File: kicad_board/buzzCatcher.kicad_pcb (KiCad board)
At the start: 2 copper layers, 63 x 100 mm, 31 parts, among them IC1 CD4043BE-NG, IC2 COM-16473, IC3 CD74HCT173E, IC4 CD4072BE, IC5 SN74LS04N, IC6 SN74LS21NE4, IC7 TS02-66-60-BK-100-SCR-D, J1 154-UL6661, J2 154-UL6661, J3 154-UL6661, J4 154-UL6661, J5 USB4130-GF-C, Q1 BS170

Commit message: Arduino version
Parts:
- removed C1, C3: 3.3 nF, SamacSys_PCB_Library:ECWH16362RJV
- removed C2: 10 uF, SamacSys_PCB_Library:CAPPRD250W65D630H900
- removed D1, D2, D3, D4, D5: LED, LED_THT:LED_D3.0mm_Horizontal_O6.35mm_Z2.0mm
- removed IC2: COM-16473, SamacSys_PCB_Library:DIP794W53P254L959H508Q8N
- removed IC3: CD74HCT173E, SamacSys_PCB_Library:DIP794W53P254L1930H508Q16N
- removed IC4: CD4072BE, SamacSys_PCB_Library:DIP794W53P254L1930H508Q14N
- removed IC5: SN74LS04N, SamacSys_PCB_Library:DIP794W53P254L1930H508Q14N
- removed IC6: SN74LS21NE4, SamacSys_PCB_Library:DIP794W53P254L1930H508Q14N
- removed IC7: TS02-66-60-BK-100-SCR-D, SamacSys_PCB_Library:TS026660BK100SCRD
- removed J5: USB4130-GF-C, SamacSys_PCB_Library:USB4130GFC
- removed R1, R8: 110k, Resistor_THT:R_Axial_DIN0207_L6.3mm_D2.5mm_P10.16mm_Horizontal
- removed R2, R3, R4, R5, R6: 300, Resistor_THT:R_Axial_DIN0207_L6.3mm_D2.5mm_P15.24mm_Horizontal
- removed R7: 0, Resistor_THT:R_Axial_DIN0207_L6.3mm_D2.5mm_P10.16mm_Horizontal
- added A1: Arduino_Nano_v3.x, Module:Arduino_Nano, F.Cu at (75.0, 99.9)
- added LED9: SSA-LXH1025GD, SamacSys_PCB_Library:SSALXH1025GD, F.Cu at (100.0, 134.5)
- added Q2: BS170, SamacSys_PCB_Library:LM431ACZ, F.Cu at (85.4, 75.6)
- added RN1: EXB2HV103JV, SamacSys_PCB_Library:EXB2HV104JV, F.Cu at (94.5, 81.5)
- added RN2: EXB2HV121JV, SamacSys_PCB_Library:EXB2HV_1, F.Cu at (91.7, 91.3)
- added RN3: EXB2HV121JV, SamacSys_PCB_Library:EXB2HV_1, F.Cu at (90.0, 81.5)
- IC1: value CD4043BE-NG -> TS02-66-60-BK-100-SCR-D; footprint SamacSys_PCB_Library:DIP794W53P254L1930H508Q16N -> SamacSys_PCB_Library:TS026660BK100SCRD
- J1, J2, J3, J4: value 154-UL6661 -> 95501-2661; footprint SamacSys_PCB_Library:154UL6661 -> SamacSys_PCB_Library:95501-2661
- moved Q1 70.0 mm to (75.3, 75.7), turned to 180 degrees
- moved S1 66.4 mm to (95.0, 71.0)
- moved LS1 51.3 mm to (80.0, 90.0)
- moved J1 42.8 mm to (60.0, 90.0), turned to -90 degrees
- moved J2 41.8 mm to (60.0, 105.2), turned to -90 degrees
- moved J3 40.7 mm to (60.0, 120.2), turned to -90 degrees
- moved J4 39.4 mm to (60.0, 134.4), turned to -90 degrees
- moved IC1 20.5 mm to (58.8, 68.8), turned to 0 degrees
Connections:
- IC1 pad 2: /listening_state* -> unconnected-(IC1-NO_2-Pad2)
- IC1 pad 3: /reset_button -> /Button 1
- IC1 pad 4: Net-(IC1-S1) -> /Vbus_5V
- J1 pad 3: /trigger_1 -> /Trigger 1
- J1 pad 4: Net-(IC5-1Y) -> Net-(Q1-SOURCE)
- J2 pad 3: /trigger_2 -> /Trigger 2
- J2 pad 4: Net-(IC5-2Y) -> Net-(Q1-SOURCE)
- J3 pad 3: /trigger_3 -> /Trigger 3
- J3 pad 4: Net-(IC5-3Y) -> Net-(Q1-SOURCE)
- J4 pad 3: /trigger_4 -> /Trigger 4
- J4 pad 4: Net-(IC5-4Y) -> Net-(Q1-SOURCE)
- Q1 pad 2: Net-(IC6-1Y) -> /Ready
- Q1 pad 3: Net-(LS1-+) -> Net-(Q1-SOURCE)
- S1 pad 2: Net-(IC6-1C) -> /Switch 1
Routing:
- net /Button 1: track 0.00 -> 107.4 mm
- net /Switch 1: track 0.00 -> 78.5 mm
- net /Trigger 1: track 0.00 -> 73.1 mm, vias 0 -> 1
- net /Buzzer: track 0.00 -> 70.1 mm, vias 0 -> 1
- net /Trigger 2: track 0.00 -> 61.8 mm, vias 0 -> 1
- net Net-(Q1-SOURCE): track 0.00 -> 60.9 mm
- net Net-(IC2-OUT): track 59.3 -> 0.00 mm
- net /Trigger 4: track 0.00 -> 58.1 mm, vias 0 -> 1
- net /Ready: track 0.00 -> 55.2 mm, vias 0 -> 1
- net /Trigger 3: track 0.00 -> 52.6 mm, vias 0 -> 1
- net Net-(IC5-1Y): track 45.3 -> 0.00 mm
- net /trigger_4: track 44.9 -> 0.00 mm
- net /trigger_1: track 44.9 -> 0.00 mm
- net /trigger_3: track 44.8 -> 0.00 mm
- net /trigger_2: track 44.6 -> 0.00 mm
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- added copper zone on B.Cu, net /Vbus_5V
- added copper zone on F.Cu, net GND
- removed copper zone on F.Cu, net /Vbus_5V
- removed copper zone on B.Cu, net GND
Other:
- board size 63 x 100 mm -> 52.5 x 80 mm
- board text removed: "Player 1"
- board text removed: "Player 2"
- board text removed: "Player 3"
- board text removed: "Player 4"
- board text removed: "Power"
- board text removed: "Ready"
- board text removed: "Reset"
- board text removed: "Sound On/Off"

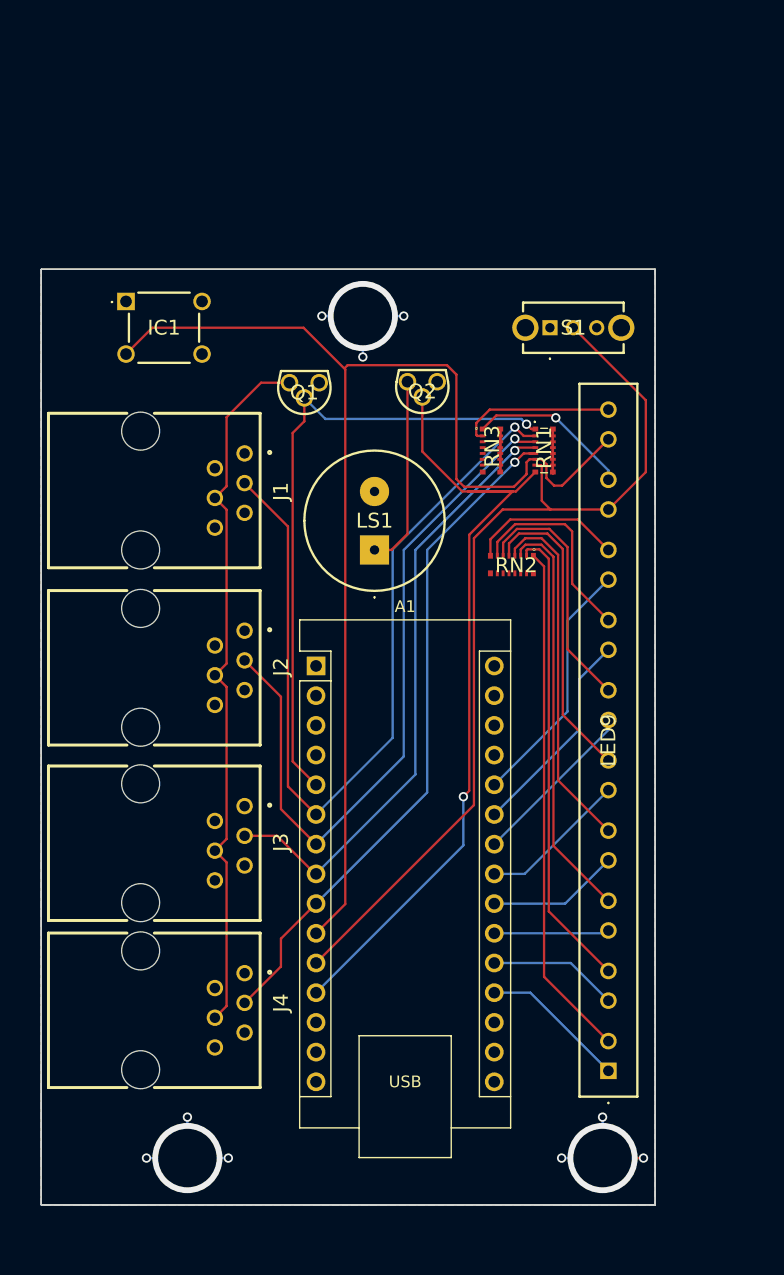
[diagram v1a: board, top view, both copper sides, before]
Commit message: Added break out headers
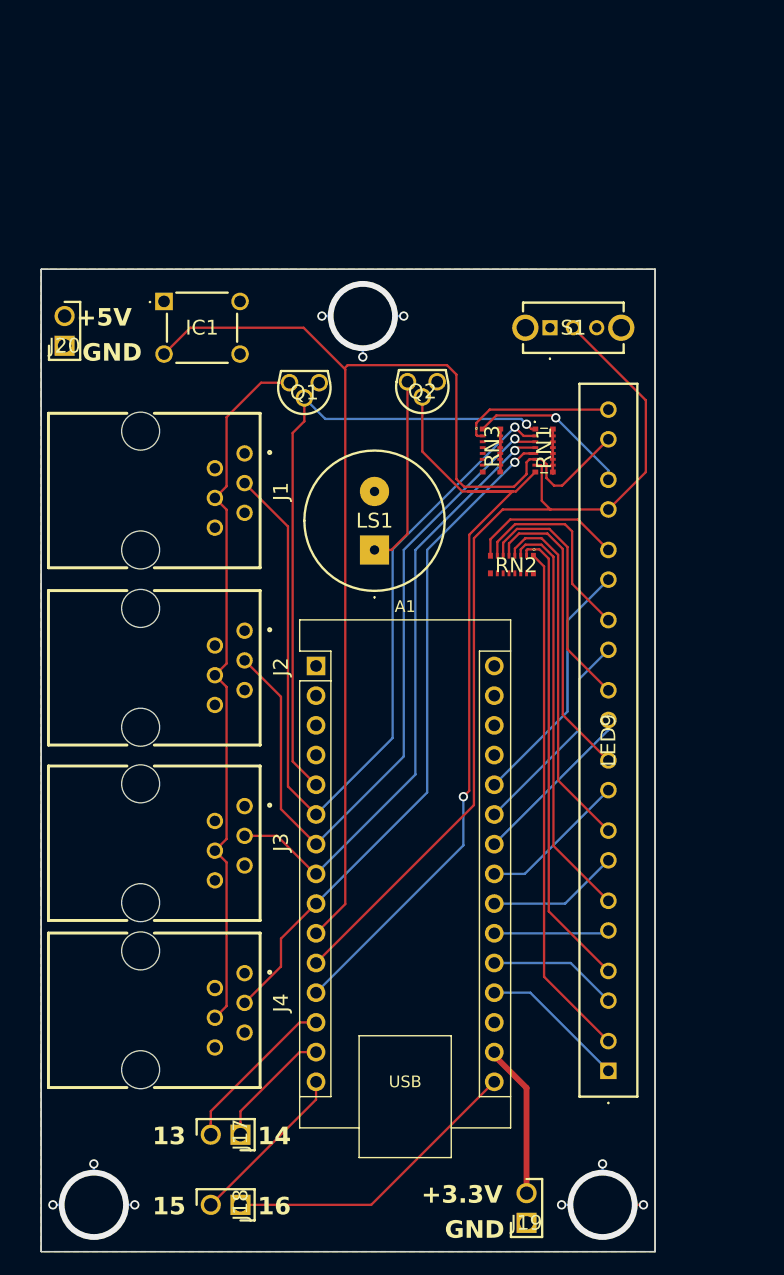
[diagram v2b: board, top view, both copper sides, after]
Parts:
- added J17: 67996-100HLF, SamacSys_PCB_Library:HDRV2W67P254_2X1_254X483X858P, F.Cu at (68.5, 140.0)
- added J18: 67996-100HLF, SamacSys_PCB_Library:HDRV2W67P254_2X1_254X483X858P, F.Cu at (68.5, 146.0)
- added J19: 67996-100HLF, SamacSys_PCB_Library:HDRV2W67P254_2X1_254X483X858P, F.Cu at (93.0, 147.5)
- added J20: 67996-100HLF, SamacSys_PCB_Library:HDRV2W67P254_2X1_254X483X858P, F.Cu at (53.5, 72.5)
- moved IC1 3.25 mm to (62.0, 68.8)
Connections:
- A1 pad 13: unconnected-(A1-D10-Pad13) -> Net-(A1-D10)
- A1 pad 14: unconnected-(A1-D11-Pad14) -> Net-(A1-D11)
- A1 pad 15: unconnected-(A1-D12-Pad15) -> Net-(A1-D12)
- A1 pad 16: unconnected-(A1-D13-Pad16) -> Net-(A1-D13)
- A1 pad 17: unconnected-(A1-3V3-Pad17) -> /Vbus_3V3
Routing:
- net Net-(A1-D13): track 0.00 -> 26.1 mm
- net Net-(A1-D10): track 0.00 -> 15.1 mm
- net Net-(A1-D12): track 0.00 -> 14.7 mm
- net /Vbus_3V3: track 0.00 -> 13.2 mm
- net Net-(A1-D11): track 0.00 -> 11.6 mm
- net /Button 1: track 107.4 -> 104.1 mm
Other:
- board size 52.5 x 80 mm -> 52.5 x 84 mm
- board text added: "+3.3V"
- board text added: "+5V"
- board text added: "13"
- board text added: "14"
- board text added: "15"
- board text added: "16"
- board text added: "GND"

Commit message: Converted to bigger resistor pack
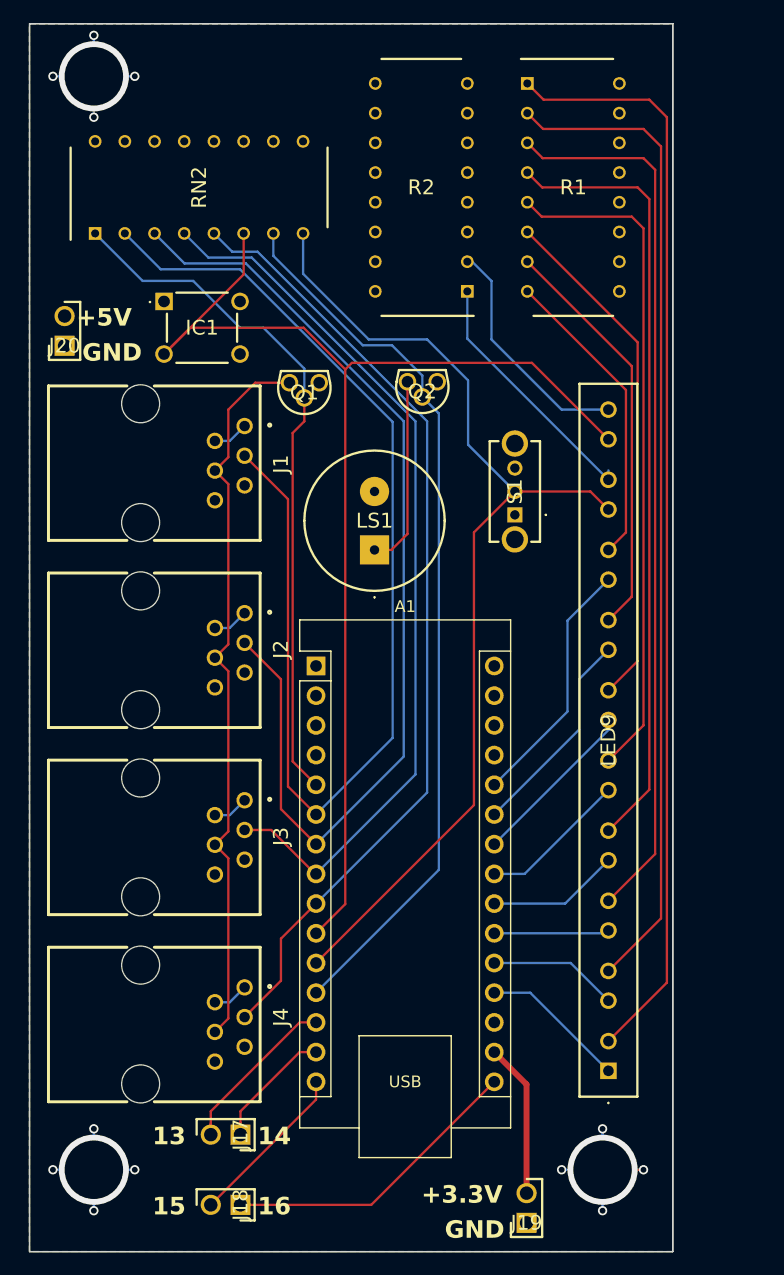
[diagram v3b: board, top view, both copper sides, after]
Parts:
- removed RN1: EXB2HV103JV, SamacSys_PCB_Library:EXB2HV104JV
- removed RN3: EXB2HV121JV, SamacSys_PCB_Library:EXB2HV_1
- added R1: 4116R-1-121LF, SamacSys_PCB_Library:DIP787W49P254L2197H469Q16N, F.Cu at (97.0, 59.0)
- added R2: 4116R-1-121LF, SamacSys_PCB_Library:DIP787W49P254L2197H469Q16N, F.Cu at (84.0, 59.0)
- RN2: value EXB2HV121JV -> 4116R-1-103FLF; footprint SamacSys_PCB_Library:EXB2HV_1 -> SamacSys_PCB_Library:DIP787W49P254L2197H469Q16N
- moved RN2 41.9 mm to (65.0, 59.0), turned to 90 degrees
- moved S1 16.3 mm to (92.0, 87.0), turned to 90 degrees
- moved J1 2.34 mm to (60.0, 87.7)
- moved J2 1.50 mm to (60.0, 103.7)
- moved J4 1.22 mm to (60.0, 135.7)
- moved J3 0.50 mm to (60.0, 119.7)
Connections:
- RN2 pad 1: Net-(LED9-K_1) -> /Ready
- RN2 pad 2: Net-(LED9-K_2) -> /Trigger 1
- RN2 pad 3: Net-(LED9-K_3) -> /Trigger 2
- RN2 pad 4: Net-(LED9-K_4) -> /Trigger 3
- RN2 pad 5: Net-(LED9-K_5) -> /Trigger 4
- RN2 pad 6: Net-(LED9-K_6) -> /Button 1
- RN2 pad 7: Net-(LED9-K_7) -> /Buzzer
- RN2 pad 8: Net-(LED9-K_8) -> /Switch 1
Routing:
- net Net-(LED9-K_1): track 44.2 -> 94.2 mm
- net Net-(LED9-K_2): track 40.1 -> 85.0 mm
- net Net-(LED9-K_3): track 35.3 -> 76.0 mm
- net Net-(LED9-K_4): track 30.6 -> 66.8 mm
- net Net-(LED9-K_5): track 26.2 -> 57.6 mm
- net /Trigger 1: track 73.1 -> 99.1 mm, vias 1 -> 0
- net /Trigger 2: track 61.8 -> 87.0 mm, vias 1 -> 0
- net /Trigger 4: track 58.1 -> 82.3 mm, vias 1 -> 0
- net /Trigger 3: track 52.6 -> 76.3 mm, vias 1 -> 0
- net Net-(LED9-K_6): track 21.4 -> 44.1 mm
- net Net-(LED9-K_7): track 17.3 -> 35.2 mm
- net GND: track 42.3 -> 57.8 mm, vias 12 -> 15
- net Net-(LED9-K_8): track 13.3 -> 26.2 mm
- net /Switch 1: track 78.5 -> 88.5 mm
- net Net-(LED9-K_9): track 14.0 -> 21.9 mm, vias 1 -> 0
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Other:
- board size 52.5 x 84 mm -> 55 x 105 mm

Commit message: Compacted to 100 x 50 mm
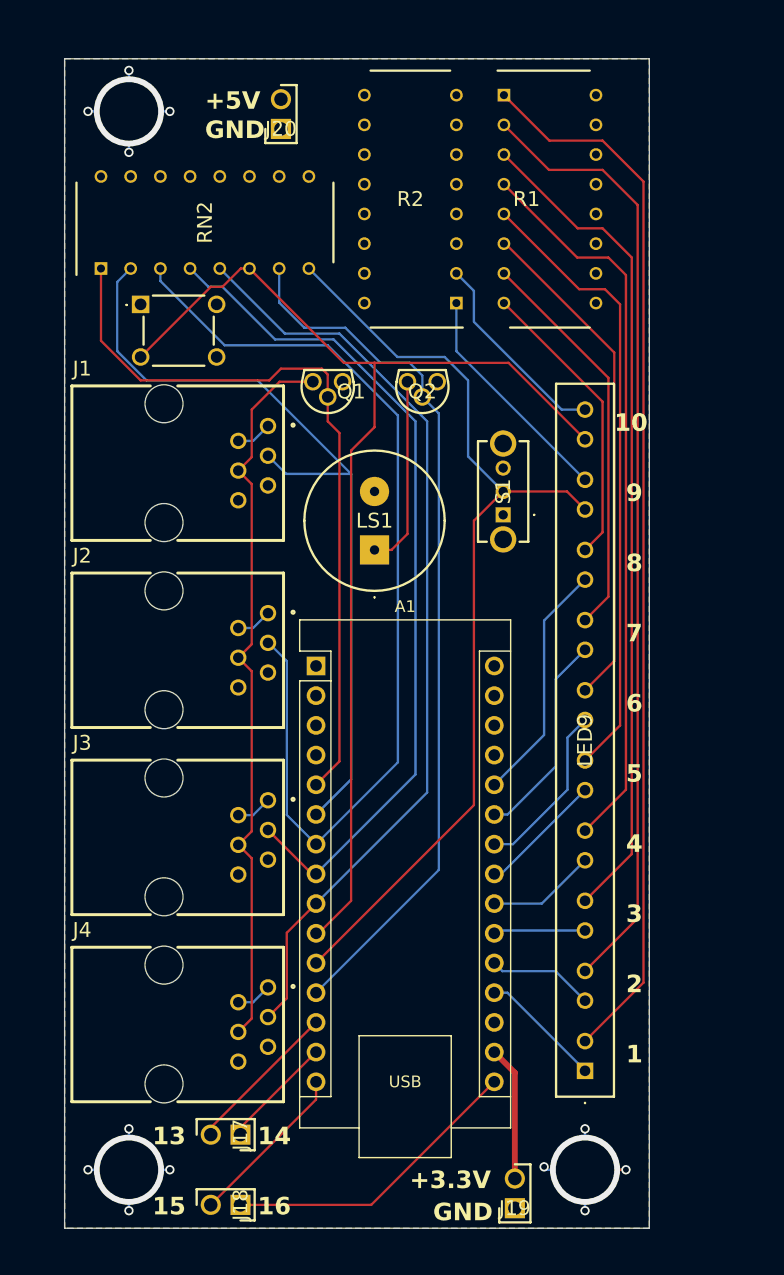
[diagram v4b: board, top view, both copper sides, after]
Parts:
- moved J20 26.2 mm to (72.0, 54.0)
- moved RN2 3.04 mm to (65.5, 62.0)
- moved R1 2.24 mm to (95.0, 60.0)
- moved IC1 2.02 mm to (60.0, 69.0)
- moved Q1 2.00 mm to (77.3, 75.6)
- moved LED9 2.00 mm to (98.0, 134.5)
- moved J1 2.00 mm to (62.0, 87.7)
- moved J2 2.00 mm to (62.0, 103.7)
- moved J3 2.00 mm to (62.0, 119.7)
- moved J4 2.00 mm to (62.0, 135.7)
- moved J19 1.60 mm to (92.0, 146.3)
- moved R2 1.37 mm to (83.1, 60.0)
- moved S1 1.00 mm to (91.0, 87.0)
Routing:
- net /Trigger 1: track 99.1 -> 70.0 mm
- net /Button 1: track 105.7 -> 97.9 mm
- net /Switch 1: track 88.5 -> 82.9 mm
- net Net-(LED9-K_3): track 76.0 -> 71.2 mm
- net /Ready: track 59.5 -> 63.9 mm
- net Net-(LED9-K_5): track 57.6 -> 53.4 mm
- net Net-(LED9-K_4): track 66.8 -> 62.6 mm
- net /Trigger 3: track 76.3 -> 72.2 mm
- net Net-(LED9-K_1): track 94.2 -> 90.6 mm
- net Net-(LED9-K_2): track 85.0 -> 81.6 mm
- net Net-(LED9-K_10): track 20.2 -> 17.4 mm
- net /LED 5: track 12.7 -> 10.1 mm
- net /Trigger 4: track 82.3 -> 79.7 mm
- net Net-(A1-D11): track 11.6 -> 9.14 mm
- net Net-(A1-D10): track 15.1 -> 12.7 mm
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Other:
- board size 55 x 105 mm -> 50 x 100 mm
- board text added: "1"
- board text added: "10"
- board text added: "2"
- board text added: "3"
- board text added: "4"
- board text added: "5"
- board text added: "6"
- board text added: "7"
- board text added: "8"
- board text added: "9"

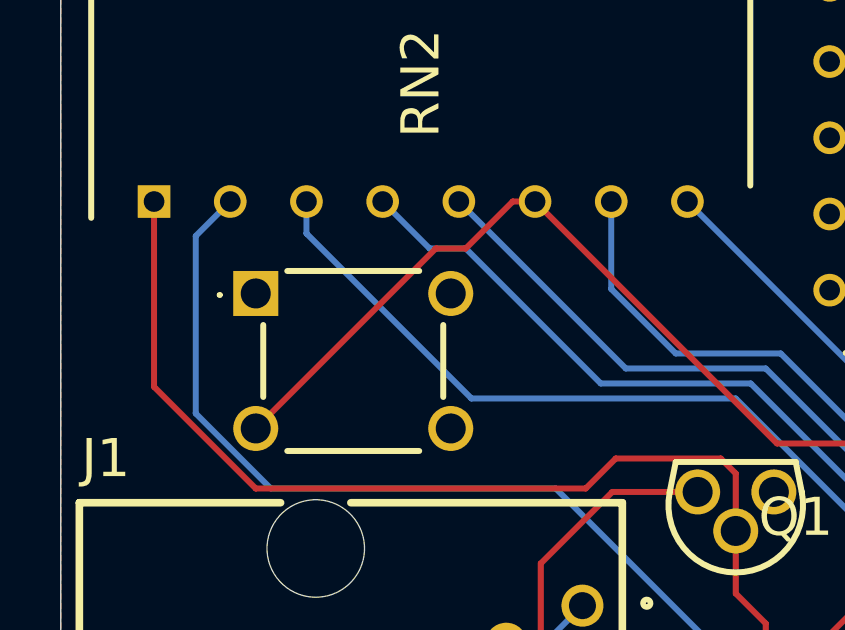
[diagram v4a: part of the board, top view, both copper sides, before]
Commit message: Fixed Version 1.0 button pin error
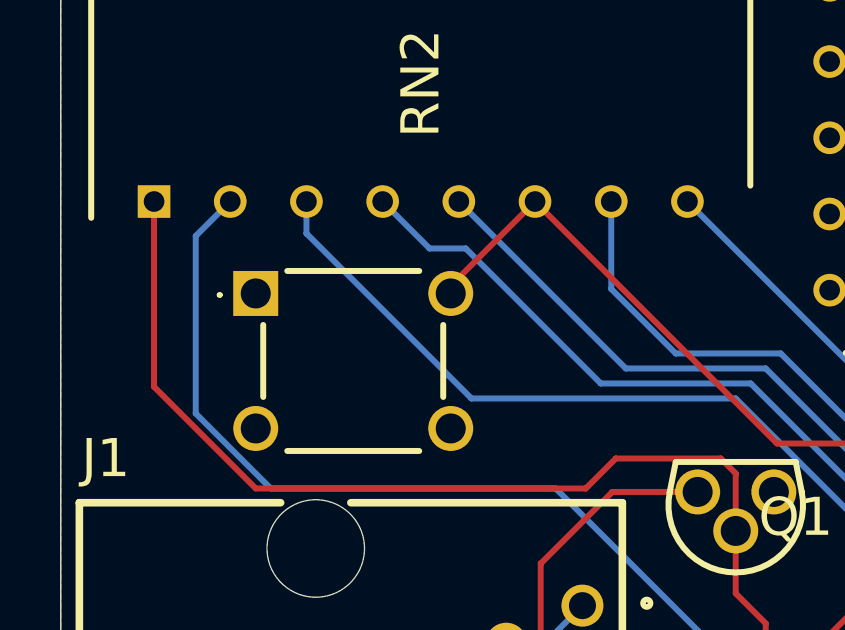
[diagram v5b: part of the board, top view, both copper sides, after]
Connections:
- IC1 pad 2: unconnected-(IC1-NO_2-Pad2) -> /Button 1
- IC1 pad 3: /Button 1 -> unconnected-(IC1-COM_1-Pad3)
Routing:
- net /Button 1: track 97.9 -> 89.7 mm
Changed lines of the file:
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@@
 	(net 29 "unconnected-(A1-D0{slash}RX-Pad2)")
 	(net 30 "unconnected-(IC1-NO_1-Pad1)")
-	(net 31 "unconnected-(IC1-NO_2-Pad2)")
+	(net 31 "unconnected-(IC1-COM_1-Pad3)")
 	(net 32 "Net-(Q1-SOURCE)")
 	(net 33 "Net-(LED9-K_4)")
@@
 		(fp_arc
 			(start 0.000001 2.600001)
-			(mid 0.049996 2.650002)
+			(mid 0.049995 2.650002)
 			(end -0.000002 2.7)
 			(stroke
@@
 			(layers "*.Cu" "*.Mask")
 			(remove_unused_layers no)
-			(net 31 "unconnected-(IC1-NO_2-Pad2)")
+			(net 9 "/Button 1")
 			(pinfunction "NO_2")
-			(pintype "passive+no_connect")
+			(pintype "passive")
 		)
 		(pad "3" thru_hole circle
@@
 			(layers "*.Cu" "*.Mask")
 			(remove_unused_layers no)
-			(net 9 "/Button 1")
+			(net 31 "unconnected-(IC1-COM_1-Pad3)")
 			(pinfunction "COM_1")
-			(pintype "passive")
+			(pintype "passive+no_connect")
 		)
 		(pad "4" thru_hole circle
@@
 	)
 	(segment
-		(start 60 73.5)
-		(end 66 67.5)
-		(width 0.2)
-		(layer "F.Cu")
-		(net 9)
-	)
-	(segment
 		(start 91.46 74)
 		(end 80 74)
@@
 	)
 	(segment
-		(start 67 67.5)
-		(end 68.564999 65.935001)
+		(start 78 120)
+		(end 78 81.5)
 		(width 0.2)
 		(layer "F.Cu")
@@
 	)
 	(segment
-		(start 78 120)
-		(end 78 81.5)
+		(start 66.5 69)
+		(end 66.5 68.745003)
 		(width 0.2)
 		(layer "F.Cu")
@@
 	)
 	(segment
-		(start 68.564999 65.935001)
-		(end 69.310002 65.935001)
-		(width 0.2)
-		(layer "F.Cu")
-		(net 9)
-	)
-	(segment
-		(start 66 67.5)
-		(end 67 67.5)
+		(start 80 79.5)
+		(end 80 74)
 		(width 0.2)
 		(layer "F.Cu")
@@
 	)
 	(segment
-		(start 80 79.5)
-		(end 80 74)
+		(start 80 74)
+		(end 77.375001 74)
 		(width 0.2)
 		(layer "F.Cu")
@@
 	)
 	(segment
-		(start 80 74)
-		(end 77.375001 74)
+		(start 66.5 68.745003)
+		(end 69.310002 65.935001)
 		(width 0.2)
 		(layer "F.Cu")
